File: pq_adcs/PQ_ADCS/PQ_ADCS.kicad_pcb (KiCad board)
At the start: 4 copper layers, 40 x 40 mm, 55 parts, among them J1 CES-110-02-L-S, J10 Pico-Clasp_01x09, J11 Pico-Clasp_01x15, J12 CES-102-02-L-S, J2 CES-110-02-L-S, J3 CES-110-02-L-S, J4 CES-110-02-L-S, J5 Conn_01x03_MountingPin, J6 Pico-Clasp_01x10, J7 Pico-Clasp_01x10, J8 Pico-Clasp_01x10, J9 Pico-Clasp_01x10, U1 LPV542, U2 LPV542, U3 LPV542, U4 IIM-42652, U5 BD2606MVV, U6 TMUX1108RSVR, U7 TCN75AVOA713

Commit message: adcs board ready for manufacturing
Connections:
- J11 pad 10: KILLSWITCH+ -> BATT-
- J11 pad 11: BATT- -> KILLSWITCH+
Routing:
- net /VCC_MAG: track 5.57 -> 94.4 mm, vias 2 -> 5
- net BURNCOMMS: track 1.33 -> 70.3 mm, vias 1 -> 3
- net SOLAR_Z: track 1.42 -> 64.1 mm, vias 1 -> 2
- net /PHT2: track 0.79 -> 57.3 mm, vias 1 -> 3
- net SOLAR_Y: track 8.69 -> 65.1 mm, vias 1 -> 3
- net SDA3: track 77.2 -> 125.7 mm, vias 4 -> 8
- net /MAG+Z: track 5.49 -> 40.5 mm
- net SCL3: track 82.8 -> 115.5 mm, vias 3 -> 8
- net /MAG-Z: track 2.97 -> 24.4 mm, vias 1 -> 2
- net /MAG-X: track 3.54 -> 22.9 mm
- net /PHT3: track 0.80 -> 19.0 mm
- net ADC_PH: track 30.1 -> 41.5 mm, vias 1 -> 0
- net 3V3_PERM: track 38.7 -> 49.4 mm, vias 12 -> 13
- net SOLAR_X: track 44.3 -> 35.3 mm, vias 0 -> 2
- net /MAG-Y: track 12.1 -> 20.0 mm, vias 1 -> 2
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- added copper zone on In4.Cu, net GND
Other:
- copper layers 4 -> 6

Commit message: files changed
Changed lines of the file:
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@@
     (fp_line (start -2 2) (end -2 -1) (layer "F.Fab") (width 0.1))
     (fp_line (start 2 -2) (end 2 2) (layer "F.Fab") (width 0.1))
-    (pad "" smd roundrect (at -0.625 0.625) (size 1.01 1.01) (layers "F.Paste") (roundrect_rratio 0.247525))
-    (pad "" smd roundrect (at 0.625 -0.625) (size 1.01 1.01) (layers "F.Paste") (roundrect_rratio 0.247525))
-    (pad "" smd roundrect (at -0.625 -0.625) (size 1.01 1.01) (layers "F.Paste") (roundrect_rratio 0.247525))
-    (pad "" smd roundrect (at 0.625 0.625) (size 1.01 1.01) (layers "F.Paste") (roundrect_rratio 0.247525))
+    (pad "" smd roundrect (at -0.625 0.625) (size 1.01 1.01) (layers "F.Paste") (roundrect_rratio 0.2475247525))
+    (pad "" smd roundrect (at 0.625 -0.625) (size 1.01 1.01) (layers "F.Paste") (roundrect_rratio 0.2475247525))
+    (pad "" smd roundrect (at -0.625 -0.625) (size 1.01 1.01) (layers "F.Paste") (roundrect_rratio 0.2475247525))
+    (pad "" smd roundrect (at 0.625 0.625) (size 1.01 1.01) (layers "F.Paste") (roundrect_rratio 0.2475247525))
     (pad "1" smd roundrect (at -1.9375 -0.975) (size 0.825 0.3) (layers "F.Cu" "F.Paste" "F.Mask") (roundrect_rratio 0.25)
       (net 50 "/MAG-X") (pinfunction "LEDA1") (pintype "unspecified"))
@@
     (pad "10" smd roundrect (at 4.5 2.025 270) (size 0.6 1.5) (layers "B.Cu" "B.Paste" "B.Mask") (roundrect_rratio 0.25)
       (net 1 "GND") (pinfunction "Pin_10") (pintype "passive"))
-    (pad "MP" smd roundrect (at 5.8 -1.875 270) (size 1.2 1.8) (layers "B.Cu" "B.Paste" "B.Mask") (roundrect_rratio 0.208333)
-      (net 1 "GND") (pinfunction "MountPin") (pintype "passive"))
-    (pad "MP" smd roundrect (at -5.8 -1.875 270) (size 1.2 1.8) (layers "B.Cu" "B.Paste" "B.Mask") (roundrect_rratio 0.208333)
+    (pad "MP" smd roundrect (at 5.8 -1.875 270) (size 1.2 1.8) (layers "B.Cu" "B.Paste" "B.Mask") (roundrect_rratio 0.2083333333)
+      (net 1 "GND") (pinfunction "MountPin") (pintype "passive"))
+    (pad "MP" smd roundrect (at -5.8 -1.875 270) (size 1.2 1.8) (layers "B.Cu" "B.Paste" "B.Mask") (roundrect_rratio 0.2083333333)
       (net 1 "GND") (pinfunction "MountPin") (pintype "passive"))
     (model "${KICAD6_3DMODEL_DIR}/Connector_Molex.3dshapes/Molex_Pico-Clasp_202396-1007_1x10-1MP_P1.00mm_Horizontal.wrl" hide
@@
     (pad "3" smd roundrect (at 1 2.025) (size 0.6 1.5) (layers "B.Cu" "B.Paste" "B.Mask") (roundrect_rratio 0.25)
       (net 29 "HEATER_PWR") (pinfunction "Pin_3") (pintype "passive"))
-    (pad "MP" smd roundrect (at 2.3 -1.875) (size 1.2 1.8) (layers "B.Cu" "B.Paste" "B.Mask") (roundrect_rratio 0.208333)
-      (net 1 "GND") (pinfunction "MountPin") (pintype "passive"))
-    (pad "MP" smd roundrect (at -2.3 -1.875) (size 1.2 1.8) (layers "B.Cu" "B.Paste" "B.Mask") (roundrect_rratio 0.208333)
+    (pad "MP" smd roundrect (at 2.3 -1.875) (size 1.2 1.8) (layers "B.Cu" "B.Paste" "B.Mask") (roundrect_rratio 0.2083333333)
+      (net 1 "GND") (pinfunction "MountPin") (pintype "passive"))
+    (pad "MP" smd roundrect (at -2.3 -1.875) (size 1.2 1.8) (layers "B.Cu" "B.Paste" "B.Mask") (roundrect_rratio 0.2083333333)
       (net 1 "GND") (pinfunction "MountPin") (pintype "passive"))
     (model "${KICAD6_3DMODEL_DIR}/Connector_Molex.3dshapes/Molex_Pico-Clasp_202396-0307_1x03-1MP_P1.00mm_Horizontal.wrl"
@@
     (pad "10" smd roundrect (at 4.5 2.025 90) (size 0.6 1.5) (layers "B.Cu" "B.Paste" "B.Mask") (roundrect_rratio 0.25)
       (net 1 "GND") (pinfunction "Pin_10") (pintype "passive"))
-    (pad "MP" smd roundrect (at 5.8 -1.875 90) (size 1.2 1.8) (layers "B.Cu" "B.Paste" "B.Mask") (roundrect_rratio 0.208333)
-      (net 1 "GND") (pinfunction "MountPin") (pintype "passive"))
-    (pad "MP" smd roundrect (at -5.8 -1.875 90) (size 1.2 1.8) (layers "B.Cu" "B.Paste" "B.Mask") (roundrect_rratio 0.208333)
+    (pad "MP" smd roundrect (at 5.8 -1.875 90) (size 1.2 1.8) (layers "B.Cu" "B.Paste" "B.Mask") (roundrect_rratio 0.2083333333)
+      (net 1 "GND") (pinfunction "MountPin") (pintype "passive"))
+    (pad "MP" smd roundrect (at -5.8 -1.875 90) (size 1.2 1.8) (layers "B.Cu" "B.Paste" "B.Mask") (roundrect_rratio 0.2083333333)
       (net 1 "GND") (pinfunction "MountPin") (pintype "passive"))
     (model "${KICAD6_3DMODEL_DIR}/Connector_Molex.3dshapes/Molex_Pico-Clasp_202396-1007_1x10-1MP_P1.00mm_Horizontal.wrl" hide
@@
     (pad "10" smd roundrect (at 4.5 2.025 90) (size 0.6 1.5) (layers "B.Cu" "B.Paste" "B.Mask") (roundrect_rratio 0.25)
       (net 1 "GND") (pinfunction "Pin_10") (pintype "passive"))
-    (pad "MP" smd roundrect (at -5.8 -1.875 90) (size 1.2 1.8) (layers "B.Cu" "B.Paste" "B.Mask") (roundrect_rratio 0.208333)
-      (net 1 "GND") (pinfunction "MountPin") (pintype "passive"))
-    (pad "MP" smd roundrect (at 5.8 -1.875 90) (size 1.2 1.8) (layers "B.Cu" "B.Paste" "B.Mask") (roundrect_rratio 0.208333)
+    (pad "MP" smd roundrect (at -5.8 -1.875 90) (size 1.2 1.8) (layers "B.Cu" "B.Paste" "B.Mask") (roundrect_rratio 0.2083333333)
+      (net 1 "GND") (pinfunction "MountPin") (pintype "passive"))
+    (pad "MP" smd roundrect (at 5.8 -1.875 90) (size 1.2 1.8) (layers "B.Cu" "B.Paste" "B.Mask") (roundrect_rratio 0.2083333333)
       (net 1 "GND") (pinfunction "MountPin") (pintype "passive"))
     (model "${KICAD6_3DMODEL_DIR}/Connector_Molex.3dshapes/Molex_Pico-Clasp_202396-1007_1x10-1MP_P1.00mm_Horizontal.wrl"
@@
     (pad "9" smd roundrect (at 4 2.025) (size 0.6 1.5) (layers "B.Cu" "B.Paste" "B.Mask") (roundrect_rratio 0.25)
       (net 30 "BURNCOMMS") (pinfunction "Pin_9") (pintype "passive"))
-    (pad "MP" smd roundrect (at -5.3 -1.875) (size 1.2 1.8) (layers "B.Cu" "B.Paste" "B.Mask") (roundrect_rratio 0.208333)
-      (net 1 "GND") (pinfunction "MountPin") (pintype "passive"))
-    (pad "MP" smd roundrect (at 5.3 -1.875) (size 1.2 1.8) (layers "B.Cu" "B.Paste" "B.Mask") (roundrect_rratio 0.208333)
+    (pad "MP" smd roundrect (at -5.3 -1.875) (size 1.2 1.8) (layers "B.Cu" "B.Paste" "B.Mask") (roundrect_rratio 0.2083333333)
+      (net 1 "GND") (pinfunction "MountPin") (pintype "passive"))
+    (pad "MP" smd roundrect (at 5.3 -1.875) (size 1.2 1.8) (layers "B.Cu" "B.Paste" "B.Mask") (roundrect_rratio 0.2083333333)
       (net 1 "GND") (pinfunction "MountPin") (pintype "passive"))
     (model "${KICAD6_3DMODEL_DIR}/Connector_Molex.3dshapes/Molex_Pico-Clasp_202396-0907_1x09-1MP_P1.00mm_Horizontal.wrl"
@@
     (pad "10" smd roundrect (at 4.5 2.025 270) (size 0.6 1.5) (layers "B.Cu" "B.Paste" "B.Mask") (roundrect_rratio 0.25)
       (net 1 "GND") (pinfunction "Pin_10") (pintype "passive"))
-    (pad "MP" smd roundrect (at 5.8 -1.875 270) (size 1.2 1.8) (layers "B.Cu" "B.Paste" "B.Mask") (roundrect_rratio 0.208333)
-      (net 1 "GND") (pinfunction "MountPin") (pintype "passive"))
-    (pad "MP" smd roundrect (at -5.8 -1.875 270) (size 1.2 1.8) (layers "B.Cu" "B.Paste" "B.Mask") (roundrect_rratio 0.208333)
+    (pad "MP" smd roundrect (at 5.8 -1.875 270) (size 1.2 1.8) (layers "B.Cu" "B.Paste" "B.Mask") (roundrect_rratio 0.2083333333)
+      (net 1 "GND") (pinfunction "MountPin") (pintype "passive"))
+    (pad "MP" smd roundrect (at -5.8 -1.875 270) (size 1.2 1.8) (layers "B.Cu" "B.Paste" "B.Mask") (roundrect_rratio 0.2083333333)
       (net 1 "GND") (pinfunction "MountPin") (pintype "passive"))
     (model "${KICAD6_3DMODEL_DIR}/Connector_Molex.3dshapes/Molex_Pico-Clasp_202396-1007_1x10-1MP_P1.00mm_Horizontal.wrl"
@@
     (pad "15" smd roundrect (at 7 2.025 180) (size 0.6 1.5) (layers "B.Cu" "B.Paste" "B.Mask") (roundrect_rratio 0.25)
       (net 37 "VCC_UMBILICAL") (pinfunction "Pin_15") (pintype "passive"))
-    (pad "MP" smd roundrect (at -8.3 -1.875 180) (size 1.2 1.8) (layers "B.Cu" "B.Paste" "B.Mask") (roundrect_rratio 0.208333)
-      (net 1 "GND") (pinfunction "MountPin") (pintype "passive"))
-    (pad "MP" smd roundrect (at 8.3 -1.875 180) (size 1.2 1.8) (layers "B.Cu" "B.Paste" "B.Mask") (roundrect_rratio 0.208333)
+    (pad "MP" smd roundrect (at -8.3 -1.875 180) (size 1.2 1.8) (layers "B.Cu" "B.Paste" "B.Mask") (roundrect_rratio 0.2083333333)
+      (net 1 "GND") (pinfunction "MountPin") (pintype "passive"))
+    (pad "MP" smd roundrect (at 8.3 -1.875 180) (size 1.2 1.8) (layers "B.Cu" "B.Paste" "B.Mask") (roundrect_rratio 0.2083333333)
       (net 1 "GND") (pinfunction "MountPin") (pintype "passive"))
     (model "${KICAD6_3DMODEL_DIR}/Connector_Molex.3dshapes/Molex_Pico-Clasp_202396-1507_1x15-1MP_P1.00mm_Horizontal.wrl"

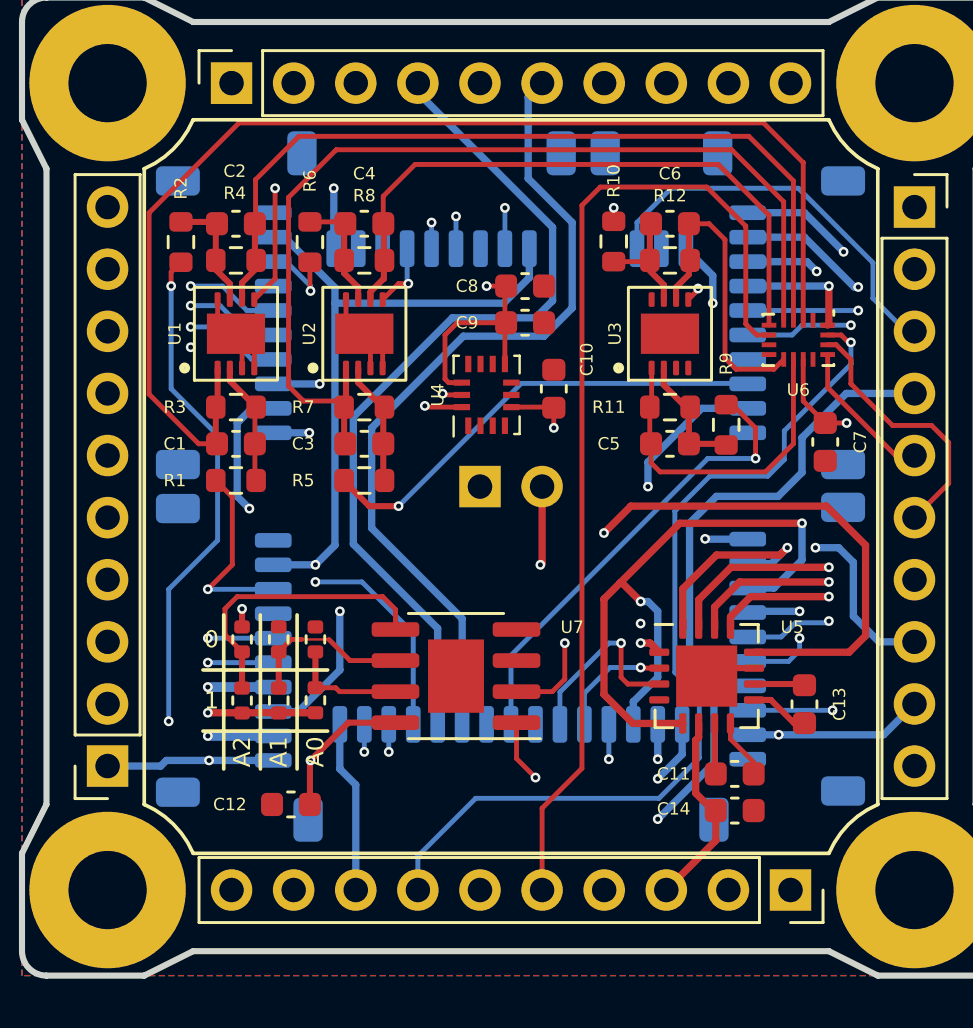
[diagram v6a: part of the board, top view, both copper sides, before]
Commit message: MTQ driver's enable connected to VCC_ADCS
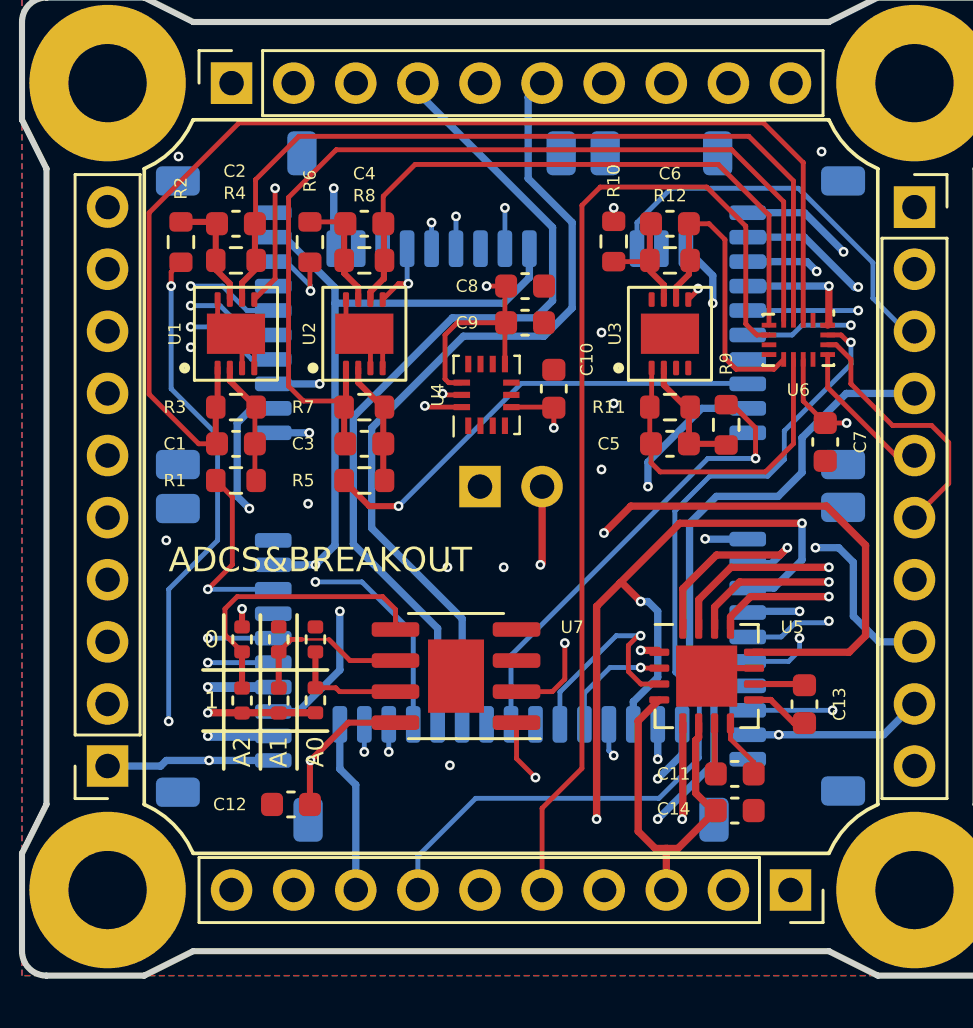
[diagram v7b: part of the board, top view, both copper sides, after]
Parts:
- J5: value Conn_01x03_MountingPin -> Pico-Clasp_01x03
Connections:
- U5 pad 4: unconnected-(U5-Pad4) -> ADCS_POWER
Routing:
- net /VCC_MAG: track 94.4 -> 104.0 mm, vias 5 -> 7
- net ADCS_POWER: track 8.11 -> 15.7 mm
- net SCL3: track 115.5 -> 117.2 mm
- net GND: vias 3 -> 12
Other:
- board text added: "ADCS&BREAKOUT"

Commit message: document formating
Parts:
- moved J7 58.3 mm to (161.7, 101.7)
- moved J8 58.3 mm to (161.7, 88.3)
- moved R9 58.3 mm to (158.8, 92.5)
- moved J10 58.3 mm to (146.8, 83.2)
- moved J5 58.3 mm to (156.2, 83.2)
- moved C1 58.3 mm to (138.8, 93.2)
- moved C10 58.3 mm to (151.8, 91.0)
- moved C11 58.3 mm to (159.2, 108.2)
- moved C12 58.3 mm to (141.0, 108.0)
- moved C13 58.3 mm to (162.0, 103.9)
- moved C14 58.3 mm to (159.2, 106.8)
- moved C2 58.3 mm to (138.8, 84.2)
- moved C3 58.3 mm to (144.0, 93.2)
- moved C4 58.3 mm to (144.0, 84.2)
- moved C5 58.3 mm to (156.5, 93.2)
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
